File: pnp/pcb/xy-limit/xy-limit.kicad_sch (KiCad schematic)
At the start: 3 parts, among them J1 Conn_01x04_Socket, SW1 X_LIM, SW2 Y_LIM

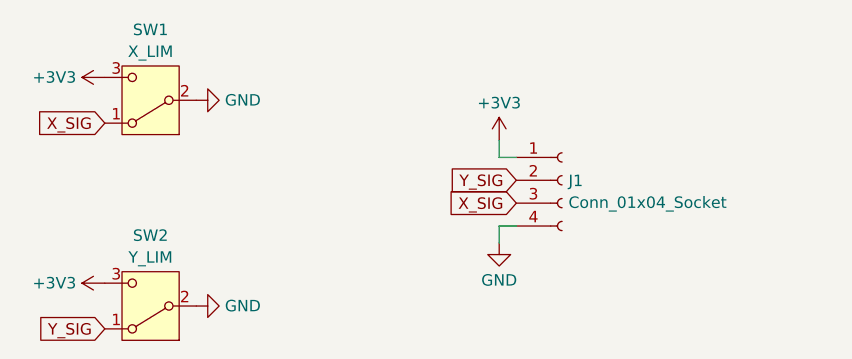
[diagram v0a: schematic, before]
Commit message: adds new xy limit and rev05b1 mobo to cad
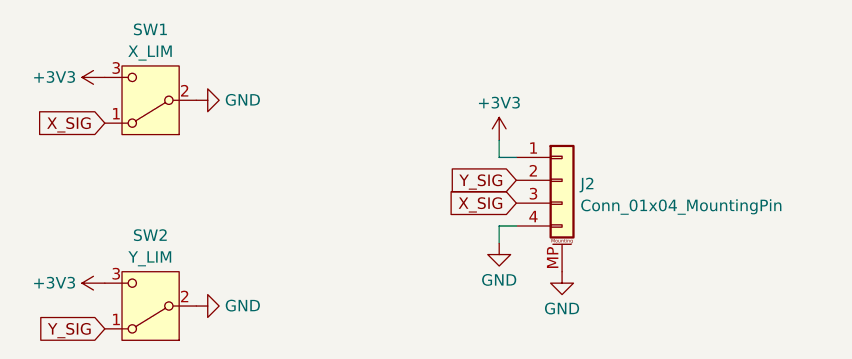
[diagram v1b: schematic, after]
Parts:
- removed J1: Conn_01x04_Socket, Connector_JST:JST_PH_B4B-PH-SM4-TB_1x04-1MP_P2.00mm_Vertical, symbol Connector:Conn_01x04_Socket
- added J2: Conn_01x04_MountingPin, Connector_JST:JST_PH_B4B-PH-SM4-TB_1x04-1MP_P2.00mm_Vertical, symbol Connector_Generic_MountingPin:Conn_01x04_MountingPin
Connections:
- net +3V3: now also J2.1 (Pin_1)
- net GND: now also J2.4 (Pin_4), J2.MP (MountPin)
- net X_SIG: now also J2.3 (Pin_3)
- net Y_SIG: now also J2.2 (Pin_2)
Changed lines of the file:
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@@
+    )
+  )
+  (symbol (lib_id "Connector_Generic_MountingPin:Conn_01x04_MountingPin") (at 181.61 74.93 0) (unit 1)
+    (in_bom yes) (on_board yes) (dnp no) (fields_autoplaced)
+    (property "Reference" "J2" (at 183.642 75.3435 0)
+      (effects (font (size 1.27 1.27)) (justify left))
+    )
+    (property "Value" "Conn_01x04_MountingPin" (at 183.642 77.7677 0)
+      (effects (font (size 1.27 1.27)) (justify left))
+    )
+    (property "Footprint" "Connector_JST:JST_PH_B4B-PH-SM4-TB_1x04-1MP_P2.00mm_Vertical" (at 181.61 74.93 0)
+      (effects (font (size 1.27 1.27)) hide)
+    )
+    (property "Datasheet" "~" (at 181.61 74.93 0)
+      (effects (font (size 1.27 1.27)) hide)
+    )
+    (pin "1")
+    (pin "3")
+    (pin "4")
+    (pin "2")
+    (pin "MP")
+    (instances
+      (project "xy-limit"
+        (path "/b41d7548-f4f8-4d41-bfe1-b9a02bb280bc"
+          (reference "J2") (unit 1)
+        )
+      )
     )
   )
@@
     )
   )
+  (symbol (lib_id "power:GND") (at 181.61 85.09 0) (unit 1)
+    (in_bom yes) (on_board yes) (dnp no) (fields_autoplaced)
+    (property "Reference" "#PWR07" (at 181.61 91.44 0)
+      (effects (font (size 1.27 1.27)) hide)
+    )
+    (property "Value" "GND" (at 181.61 89.2231 0)
+      (effects (font (size 1.27 1.27)))
+    )
+    (property "Footprint" "" (at 181.61 85.09 0)
+      (effects (font (size 1.27 1.27)) hide)
+    )
+    (property "Datasheet" "" (at 181.61 85.09 0)
+      (effects (font (size 1.27 1.27)) hide)
+    )
+    (pin "1")
+    (instances
+      (project "xy-limit"
+        (path "/b41d7548-f4f8-4d41-bfe1-b9a02bb280bc"
+          (reference "#PWR07") (unit 1)
+        )
+      )
+    )
+  )
   (symbol (lib_id "power:+3V3") (at 130.81 86.36 90) (unit 1)
     (in_bom yes) (on_board yes) (dnp no) (fields_autoplaced)
@@
         )
       )
-    )
-  )
-  (symbol (lib_id "Connector:Conn_01x04_Socket") (at 181.61 74.93 0) (unit 1)
-    (in_bom yes) (on_board yes) (dnp no) (fields_autoplaced)
-    (property "Reference" "J1" (at 182.3212 74.9879 0)
-      (effects (font (size 1.27 1.27)) (justify left))
-    )
-    (property "Value" "Conn_01x04_Socket" (at 182.3212 77.4121 0)
-      (effects (font (size 1.27 1.27)) (justify left))
-    )
-    (property "Footprint" "Connector_JST:JST_PH_B4B-PH-SM4-TB_1x04-1MP_P2.00mm_Vertical" (at 181.61 74.93 0)
-      (effects (font (size 1.27 1.27)) hide)
-    )
-    (property "Datasheet" "~" (at 181.61 74.93 0)
-      (effects (font (size 1.27 1.27)) hide)
-    )
-    (pin "1")
-    (pin "3")
-    (pin "4")
-    (pin "2")
-    (instances
-      (project "xy-limit"
-        (path "/b41d7548-f4f8-4d41-bfe1-b9a02bb280bc"
-          (reference "J1") (unit 1)
-        )
-      )

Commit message: updates with all current v4 pcbs
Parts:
- J2: LCSC Part Number (none) -> C2845453; MFG Part Number (none) -> HC-PH-4ALT
- SW1: LCSC Part Number (none) -> C466018; MFG Part Number (none) -> DM1-12UC-1
- SW2: LCSC Part Number (none) -> C405946; MFG Part Number (none) -> DM1-135P-1
